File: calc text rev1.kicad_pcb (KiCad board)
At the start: 4 copper layers, 65 x 97.8 mm, 31 parts, among them J1 Conn_ARM_SWD_TagConnect_TC203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, U1 STM32WL5MOCH6STR, U2 TLV75533PDBV

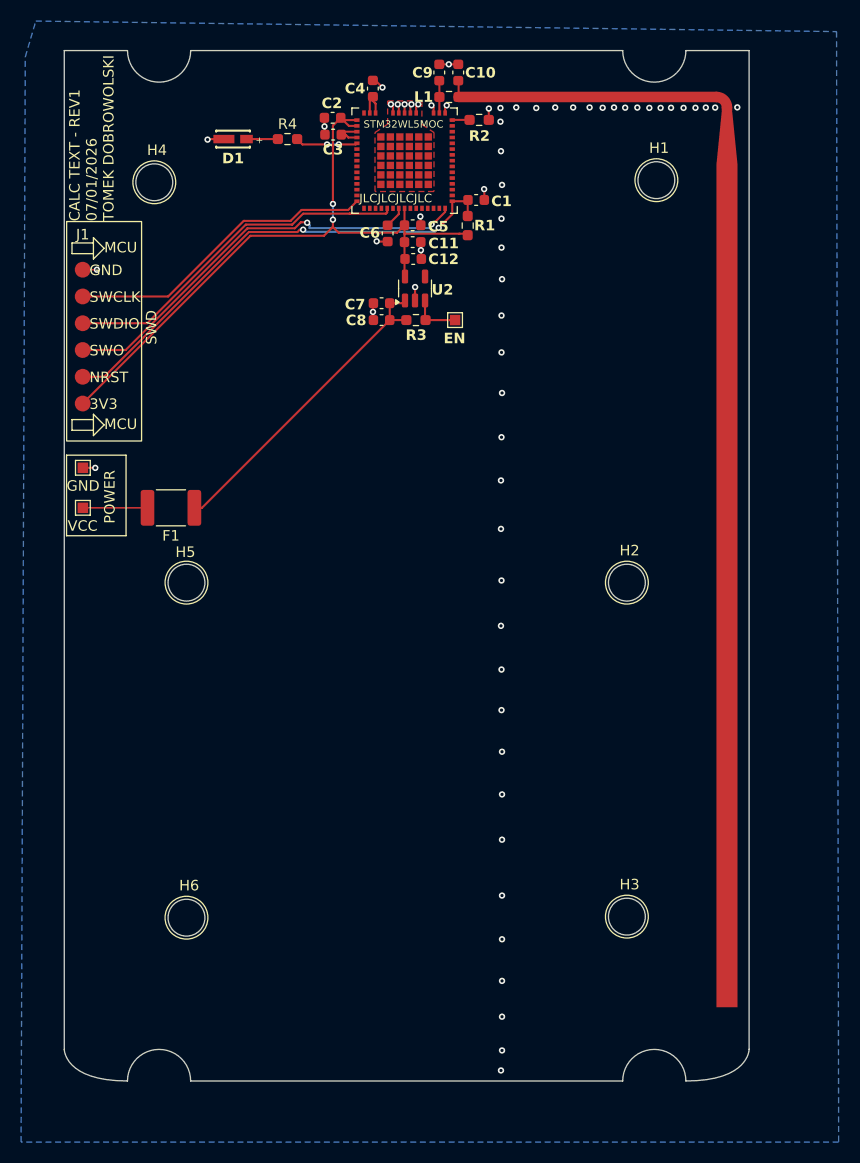
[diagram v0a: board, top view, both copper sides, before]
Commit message: fix: move mounting holes
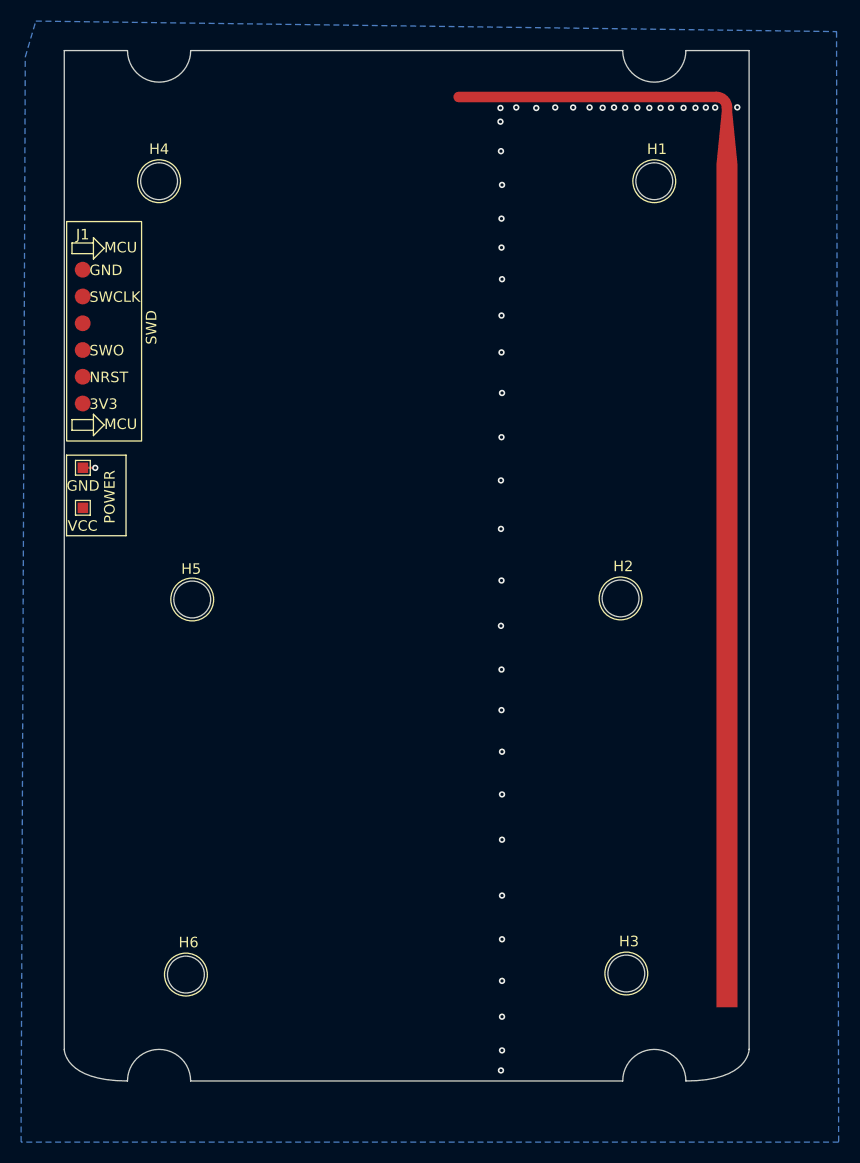
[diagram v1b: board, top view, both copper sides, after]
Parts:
- removed C1, C10, C12, C2, C3, C4, C5, C6, C7, C9: 100nF, Capacitor_SMD:C_0603_1608Metric
- removed C11, C8: 4.7uF, Capacitor_SMD:C_0603_1608Metric
- removed D1: WL-SWTP_3014, 158301260:WL-SWTP_3014
- removed F1: 0603L150SLYR, Fuse:Fuse_1812_4532Metric_Pad1.30x3.40mm_HandSolder
- removed L1: 0R, Resistor_SMD:R_0603_1608Metric_Pad0.98x0.95mm_HandSolder
- removed R1, R2, R3: 10k, Resistor_SMD:R_0603_1608Metric_Pad0.98x0.95mm_HandSolder
- removed R4: 1k, Resistor_SMD:R_0603_1608Metric_Pad0.98x0.95mm_HandSolder
- removed TP1: EN, TestPoint:TestPoint_Pad_1.0x1.0mm
- removed U1: STM32WL5MOCH6STR, STM32WL5MOCH6STR:XCVR_STM32WL5MOCH6STR
- removed U2: TLV75533PDBV, Package_TO_SOT_SMD:SOT-23-5
- moved H3 5.40 mm to (70.5, 104.4)
- moved H6 5.40 mm to (28.7, 104.5)
- moved H5 1.69 mm to (29.3, 68.9)
- moved H2 1.62 mm to (70.0, 68.8)
- moved H4 0.46 mm to (26.2, 29.2)
- moved H1 0.22 mm to (73.2, 29.2)
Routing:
- net +3.3V: track 65.1 -> 0.00 mm, vias 2 -> 0
- net Net-(J1-~{RESET}): track 46.0 -> 0.00 mm, vias 2 -> 0
- net Net-(J1-SWO): track 40.9 -> 0.00 mm, vias 2 -> 0
- net Net-(J1-SWCLK): track 33.6 -> 0.00 mm
- net Net-(U2-IN): track 30.7 -> 0.00 mm
- net Net-(J1-SWDIO): track 29.8 -> 0.00 mm
- net GND: track 23.6 -> 1.18 mm, vias 63 -> 44
- net +4.2V: track 6.14 -> 0.00 mm
- net unconnected-(R4-Pad2): track 5.93 -> 0.00 mm, vias 2 -> 0
- net Net-(U2-EN): track 4.68 -> 0.00 mm
- net Net-(U1-BIAS_LP): track 3.32 -> 0.00 mm
- net Net-(U1-VDDPA): track 3.19 -> 0.00 mm
- net Net-(U1-ANT): track 3.08 -> 0.00 mm
- net Net-(D1-Pad2): track 2.97 -> 0.00 mm
- net Net-(U1-VREF+): track 2.04 -> 0.00 mm
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- removed copper zone on F.Cu, net GND
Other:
- board text removed: "C1"
- board text removed: "C10"
- board text removed: "C11"
- board text removed: "C12"
- board text removed: "C2"
- board text removed: "C3"
- board text removed: "C4"
- board text removed: "C5"
- board text removed: "C6"
- board text removed: "C7"
- board text removed: "C8"
- board text removed: "C9"
- board text removed: "CALC TEXT - REV1 07/01/2026 TOMEK DOBROWOLSKI"
- board text removed: "EN"
- board text removed: "JLCJLCJLCJLC"
- board text removed: "L1"
- board text removed: "R1"
- board text removed: "R2"
- board text removed: "R3"
- board text removed: "STM32WL5MOC"
- board text removed: "U2"

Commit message: fix: move bottom holes up 2.7 right 1.0mm
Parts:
- moved H6 2.88 mm to (29.7, 101.8)
- moved H3 2.86 mm to (71.5, 101.7)
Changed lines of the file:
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@@
 	(footprint "MountingHole:MountingHole_3.5mm_CustomFilled"
 		(layer "F.Cu")
-		(at 70.5 104.4)
+		(at 71.454 101.7)
 		(descr "Mounting Hole 2.1mm, no annular, generated by kicad-footprint-generator mountinghole.py")
 		(tags "mountinghole")
 		(property "Reference" "H3"
-			(at 0 -3.05 0)
+			(at -0.3 -3.05 0)
 			(layer "F.SilkS")
 			(effects
@@
 	(footprint "MountingHole:MountingHole_3.5mm_CustomFilled"
 		(layer "F.Cu")
-		(at 28.7 104.5)
+		(at 29.7 101.8)
 		(descr "Mounting Hole 2.1mm, no annular, generated by kicad-footprint-generator mountinghole.py")
 		(tags "mountinghole")
 		(property "Reference" "H6"
-			(at 0 -3.05 0)
-			(layer "F.SilkS")
-			(effects
+			(at -0.2 -3.1 0)
+			(layer "F.SilkS")
+			(effects

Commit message: refactor: remove most of annoying fab marks
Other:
- outline, holes or cut-outs redrawn
- board text removed: "0Ω"
- board text removed: "100nF"
- board text removed: "10kΩ"
- board text removed: "4.7kF"
